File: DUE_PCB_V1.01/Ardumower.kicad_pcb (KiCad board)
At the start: 2 copper layers, 169.2 x 95.5 mm, 82 parts, among them J1 I2C_1, J10 P_Left, J11 P_Right, J12 Sonar_R, J13 Sonar_C, J14 Sonar_L, J15 Bumper Left, J16 Button, J17 US1, J18 US3, J19 US3, J2 I2C_2, J20 5V IN, J21 Remote, J22 PCB_2, J23 5V, J24 3.3V IN, J25 3.3V, J26 GND, J27 RX & TX, J28 Motor Left, J29 Cutter Motor, J3 I2C_3, J30 Motor Right, J31 Bumper Right, J4 DS3231 RTC, J5 9V IN, J6 Drop_Left, J7 Drop_Right, J8 Tilt, J9 Rain, U1 MC33926, U2 MC33926

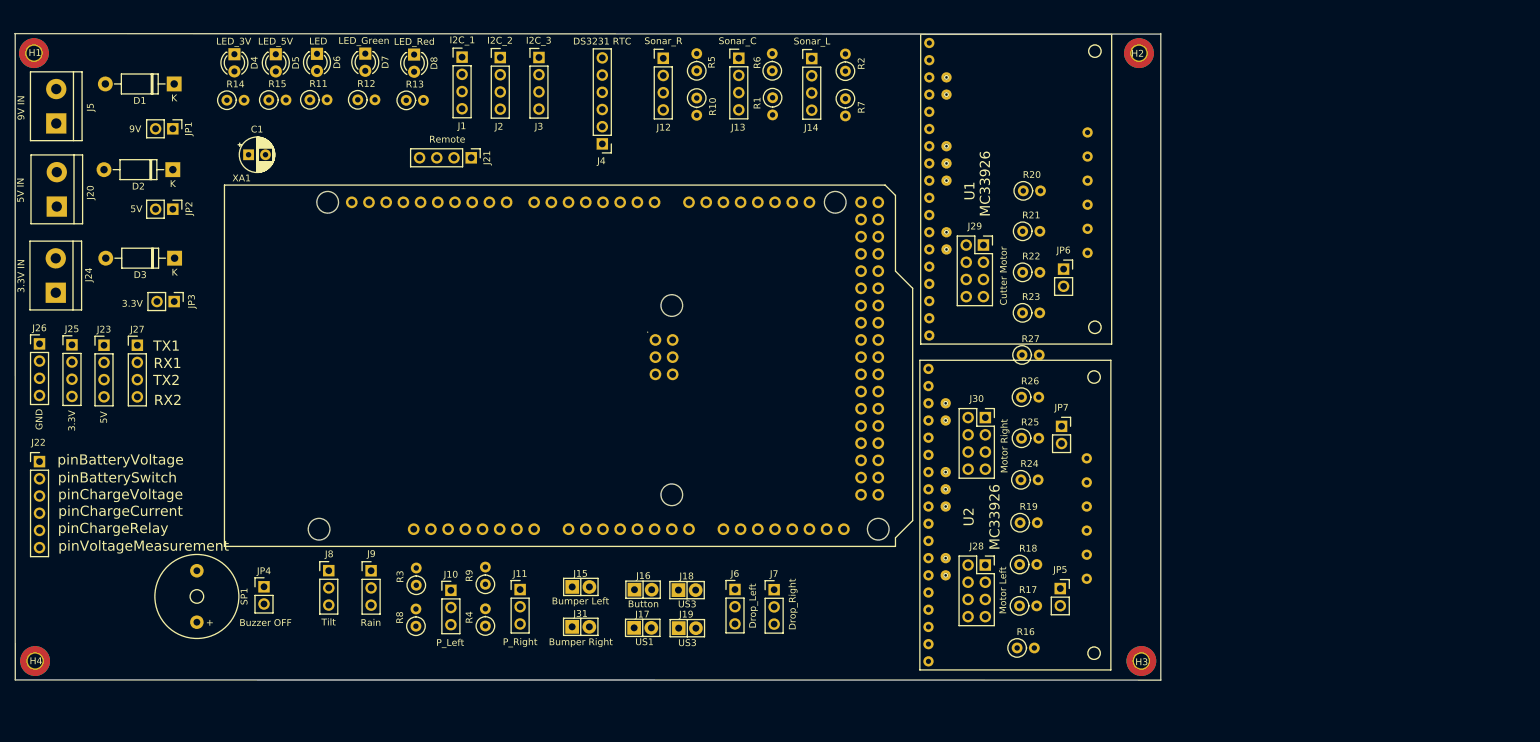
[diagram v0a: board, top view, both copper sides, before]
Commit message: Ad new RX TX Connector and some other improvements
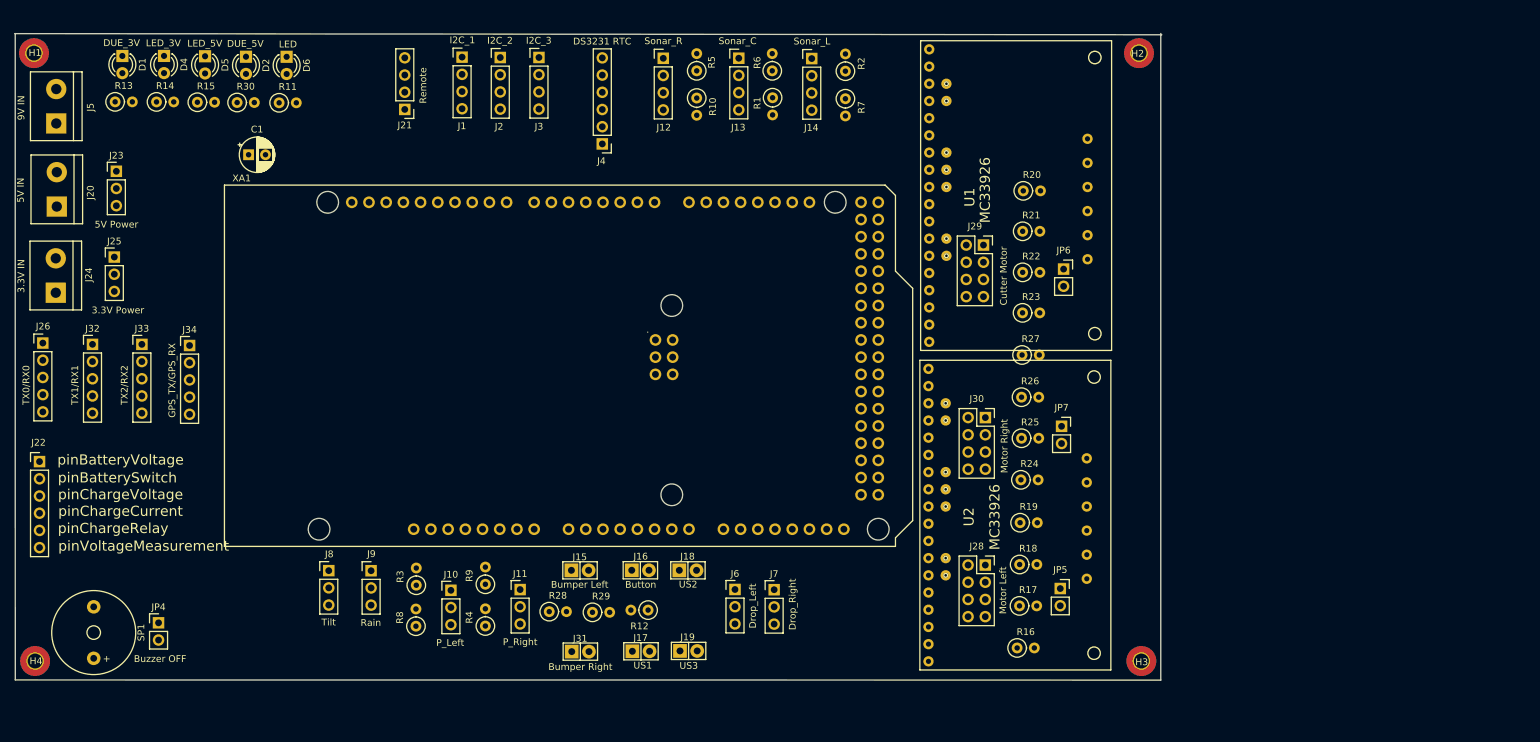
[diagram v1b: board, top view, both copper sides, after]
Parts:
- removed D3: 1N5819, Diode_THT:D_DO-41_SOD81_P10.16mm_Horizontal
- removed D7: LED_Green, LED_THT:LED_D3.0mm
- removed D8: LED_Red, LED_THT:LED_D3.0mm
- removed J27: RX & TX, Connector_PinHeader_2.54mm:PinHeader_1x04_P2.54mm_Vertical
- removed JP1: 9V, Connector_PinHeader_2.54mm:PinHeader_1x02_P2.54mm_Vertical
- removed JP2: 5V, Connector_PinHeader_2.54mm:PinHeader_1x02_P2.54mm_Vertical
- removed JP3: 3.3V, Connector_PinHeader_2.54mm:PinHeader_1x02_P2.54mm_Vertical
- added J32: TX1/RX1, Connector_PinHeader_2.54mm:PinHeader_1x05_P2.54mm_Vertical, F.Cu at (50.6, 81.4)
- added J33: TX2/RX2, Connector_PinHeader_2.54mm:PinHeader_1x05_P2.54mm_Vertical, F.Cu at (57.9, 81.4)
- added J34: GPS_TX/GPS_RX, Connector_PinHeader_2.54mm:PinHeader_1x05_P2.54mm_Vertical, F.Cu at (65.0, 81.5)
- added R28: 10k, Resistor_THT:R_Axial_DIN0207_L6.3mm_D2.5mm_P2.54mm_Vertical, F.Cu at (118.1, 120.8)
- added R29: 10k, Resistor_THT:R_Axial_DIN0207_L6.3mm_D2.5mm_P2.54mm_Vertical, F.Cu at (124.4, 120.9)
- added R30: 220, Resistor_THT:R_Axial_DIN0207_L6.3mm_D2.5mm_P2.54mm_Vertical, F.Cu at (72.0, 45.7)
- D1: value 1N5819 -> DUE_3V; footprint Diode_THT:D_DO-41_SOD81_P10.16mm_Horizontal -> LED_THT:LED_D3.0mm
- D2: value 1N5819 -> DUE_5V; footprint Diode_THT:D_DO-41_SOD81_P10.16mm_Horizontal -> LED_THT:LED_D3.0mm
- J18: value US3 -> US2
- J23: value 5V -> 5V Power; footprint Connector_PinHeader_2.54mm:PinHeader_1x04_P2.54mm_Vertical -> Connector_PinHeader_2.54mm:PinHeader_1x03_P2.54mm_Vertical
- J25: value 3.3V -> 3.3V Power; footprint Connector_PinHeader_2.54mm:PinHeader_1x04_P2.54mm_Vertical -> Connector_PinHeader_2.54mm:PinHeader_1x03_P2.54mm_Vertical
- J26: value GND -> TX0/RX0; footprint Connector_PinHeader_2.54mm:PinHeader_1x04_P2.54mm_Vertical -> Connector_PinHeader_2.54mm:PinHeader_1x05_P2.54mm_Vertical
- R12: value 100 -> 10k
- moved R12 86.7 mm to (132.7, 120.6), turned to 180 degrees
- moved R13 43.0 mm to (54.0, 45.6)
- moved J23 25.7 mm to (54.1, 55.8)
- moved D2 19.9 mm to (73.3, 38.9), turned to 270 degrees
- moved JP4 16.5 mm to (60.4, 122.5)
- moved SP1 16.1 mm to (50.8, 123.9)
- moved J25 14.4 mm to (53.9, 68.5)
- moved J21 12.1 mm to (96.7, 46.7), turned to 180 degrees
- moved R15 10.6 mm to (66.1, 45.6)
- moved D5 10.4 mm to (67.2, 38.9)
- moved D4 10.4 mm to (61.2, 38.8)
- moved R14 10.4 mm to (60.1, 45.6)
- moved D1 8.69 mm to (55.0, 38.8), turned to 270 degrees
- moved R11 4.56 mm to (78.2, 45.7)
- moved D6 4.50 mm to (79.3, 38.9)
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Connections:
- D1 pad 1: Net-(D1-Pad1) -> GND
- D2 pad 1: Net-(D2-Pad1) -> GND
- J1 pad 1: +3.3VA -> +3V3
- J10 pad 1: +5VA -> +5V
- J11 pad 1: +5VA -> +5V
- J12 pad 1: +5VA -> +5V
- J13 pad 1: +5VA -> +5V
- J14 pad 1: +5VA -> +5V
- J2 pad 1: +3.3VA -> +3V3
- J20 pad 2: Net-(D2-Pad2) -> +5VA
- J23 pad 1: +5VA -> DUE_5V
- J23 pad 2: +5VA -> +5V
- J24 pad 2: Net-(D3-Pad2) -> +3.3VA
- J25 pad 1: +3.3VA -> DUE_3.3V
- J25 pad 2: +3.3VA -> +3V3
- J26 pad 1: GND -> +3V3
- J26 pad 3: GND -> RX0
- J26 pad 4: GND -> TX0
- J3 pad 1: +3.3VA -> +3V3
- J4 pad 5: +3.3VA -> +3V3
- J5 pad 2: Net-(D1-Pad2) -> +9V
- J6 pad 1: +3.3VA -> +3V3
- J7 pad 1: +3.3VA -> +3V3
- J8 pad 1: +3.3VA -> +3V3
- J9 pad 1: +3.3VA -> +3V3
- R12 pad 1: pinGreenLED -> pinButton
- R12 pad 2: Net-(D7-Pad2) -> GND
- R13 pad 1: pinRedLED -> Net-(D1-Pad2)
- R13 pad 2: Net-(D8-Pad2) -> DUE_3.3V
- XA1 pad 3V3: (no net) -> DUE_3.3V
- XA1 pad 5V1: (no net) -> DUE_5V
- XA1 pad D0: (no net) -> RX0
- XA1 pad D1: (no net) -> TX0
- XA1 pad D14: (no net) -> GPS_RX
- XA1 pad D15: (no net) -> GPS_TX
- XA1 pad D6: pinGreenLED -> pinFrontMotorLeft
- XA1 pad D7: pinRedLED -> pinFrontMotorLeft
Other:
- board size 169.2 x 95.5 mm -> 169.3 x 95.5 mm
- board text removed: "RX1"
- board text removed: "RX2"
- board text removed: "TX1"
- board text removed: "TX2"

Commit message: Change Connector Type
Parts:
- D1: value DUE_3V -> LED_DUE_3V
- D2: value DUE_5V -> LED_DUE_5V
- J15: footprint Zimprich:Pin_Header_KK110_1x02_3D -> Connector_PinHeader_2.54mm:PinHeader_1x02_P2.54mm_Vertical

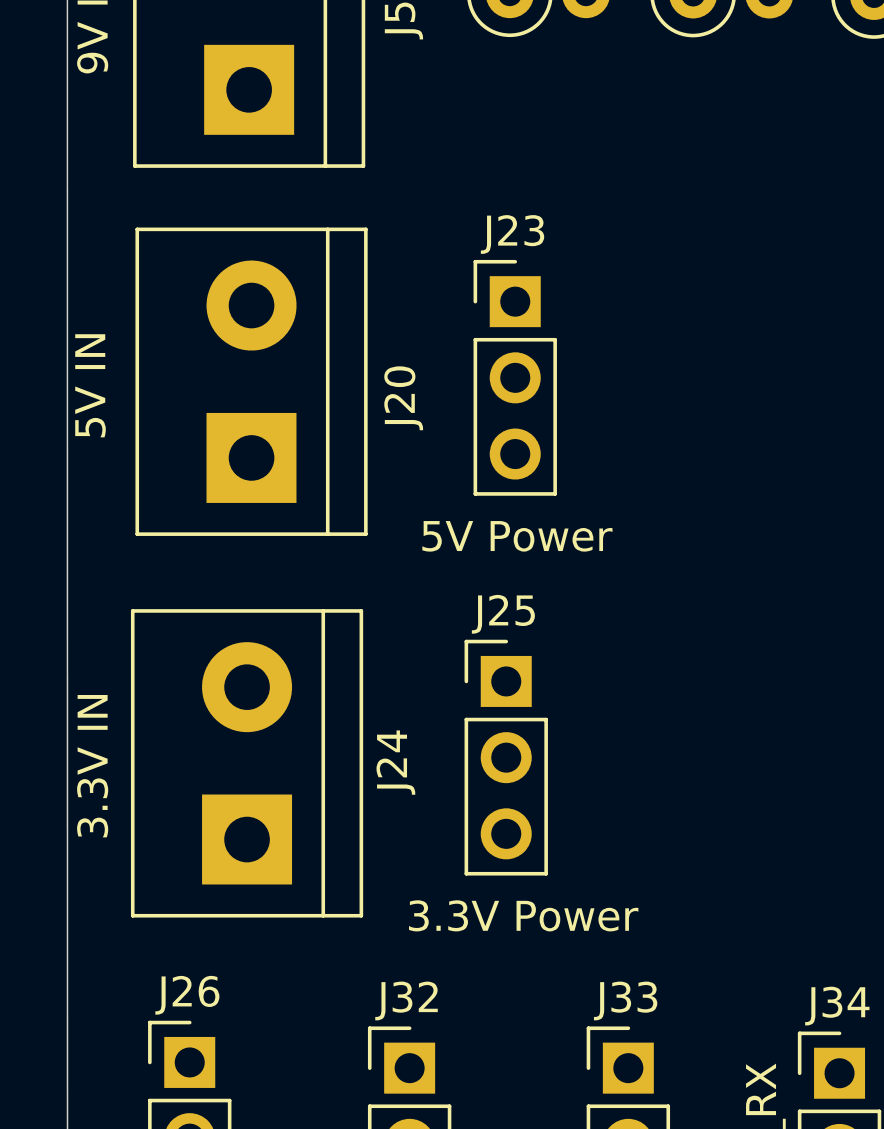
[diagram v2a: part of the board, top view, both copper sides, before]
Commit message: Change Jumper for Power Source
Change Screw Terminal for 5V/3.3V to jumper.
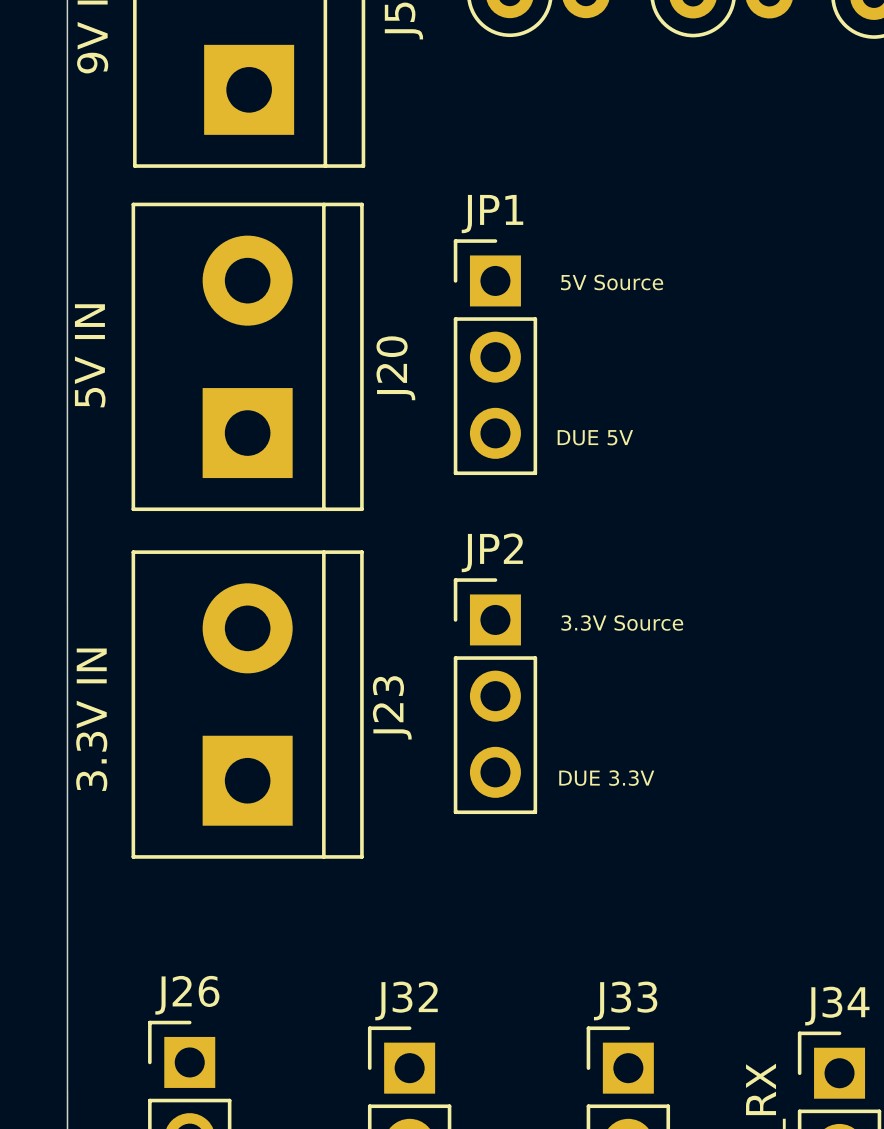
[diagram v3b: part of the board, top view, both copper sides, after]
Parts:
- removed J24: 3.3V IN, TerminalBlock:TerminalBlock_bornier-2_P5.08mm
- removed J25: 3.3V Power, Connector_PinHeader_2.54mm:PinHeader_1x03_P2.54mm_Vertical
- added JP1: Jumper_5V, Connector_PinHeader_2.54mm:PinHeader_1x03_P2.54mm_Vertical, F.Cu at (53.5, 55.1)
- added JP2: Jumper_3.3V, Connector_PinHeader_2.54mm:PinHeader_1x03_P2.54mm_Vertical, F.Cu at (53.5, 66.4)
- J23: value 5V Power -> 3.3V IN; footprint Connector_PinHeader_2.54mm:PinHeader_1x03_P2.54mm_Vertical -> TerminalBlock:TerminalBlock_bornier-2_P5.08mm
- moved J23 18.3 mm to (45.2, 71.8), turned to 90 degrees
- moved J20 0.84 mm to (45.2, 60.2)
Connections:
- J20 pad 2: +5VA -> Net-(J20-Pad2)
- J23 pad 1: DUE_5V -> GND
- J23 pad 2: +5V -> Net-(J23-Pad2)
- R14 pad 2: +3.3VA -> (no net)
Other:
- board text added: "3.3V Source"
- board text added: "5V Source"
- board text added: "DUE 3.3V"
- board text added: "DUE 5V"

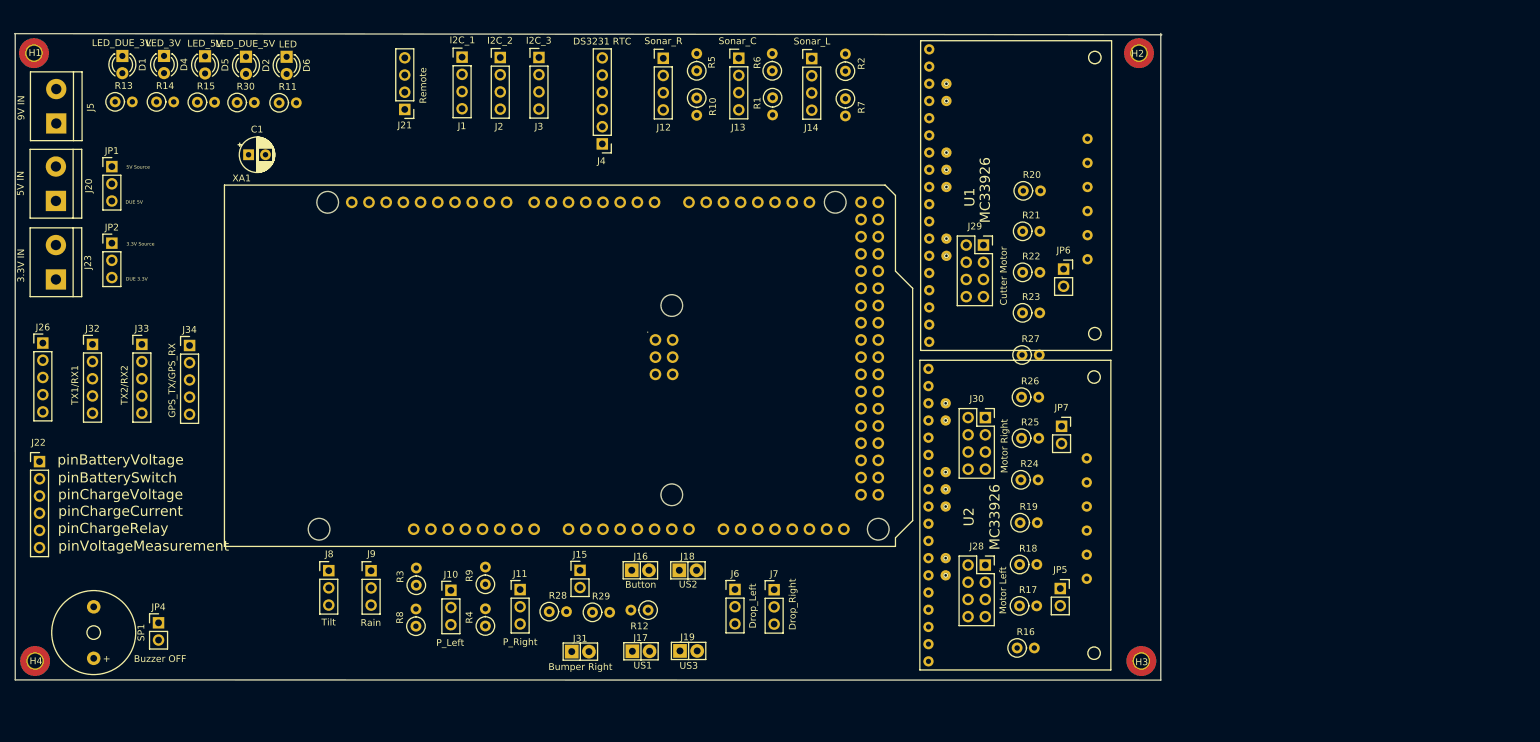
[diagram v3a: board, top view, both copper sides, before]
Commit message: Change LED Power Source
Change the Power Source from the LED_5V and LED_3.3V
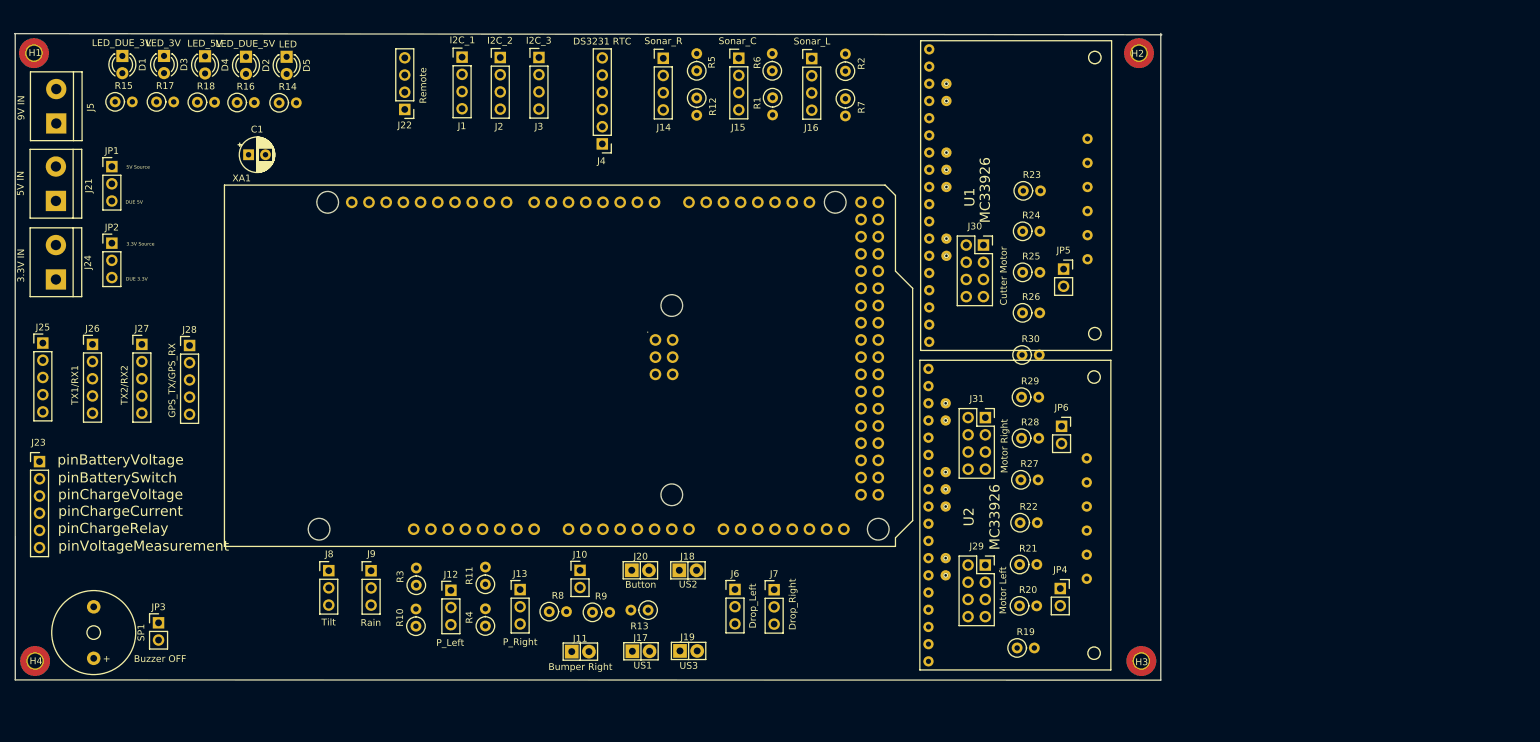
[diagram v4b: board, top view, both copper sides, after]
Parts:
- renumbered D4 to D3, D5 to D4, D6 to D5, J15 to J10, J31 to J11, J10 to J12, J11 to J13, J12 to J14, J13 to J15, J14 to J16, J16 to J20, J20 to J21, J21 to J22, J22 to J23, J23 to J24, J26 to J25, J32 to J26, J33 to J27, J34 to J28, J28 to J29, J29 to J30, J30 to J31, JP4 to JP3, JP5 to JP4, JP6 to JP5, JP7 to JP6, R8 to R10, R9 to R11, R10 to R12, R12 to R13, R11 to R14, R13 to R15, R30 to R16, R14 to R17, R15 to R18, R16 to R19, R17 to R20, R18 to R21, R19 to R22, R20 to R23, R21 to R24, R22 to R25, R23 to R26, R24 to R27, R25 to R28, R26 to R29, R27 to R30, R28 to R8, R29 to R9
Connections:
- R17 pad 2: (no net) -> +3V3
- R18 pad 2: +5VA -> +5V
